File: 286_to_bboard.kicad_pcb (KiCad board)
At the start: 2 copper layers, 33.5 x 78.7 mm, 28 parts, among them J1 Conn_01x30, J2 Conn_01x30, J3 Conn_01x02, U1 74HC244

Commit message: finalize initial design
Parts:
- added C6: C, Capacitor_SMD:C_0805_2012Metric_Pad1.18x1.45mm_HandSolder, F.Cu at (157.7, 70.6)
- C1, C2, C3, C4: footprint Capacitor_SMD:C_0805_2012Metric -> Capacitor_SMD:C_0805_2012Metric_Pad1.18x1.45mm_HandSolder
- C5: footprint Capacitor_SMD:C_0402_1005Metric -> Capacitor_SMD:C_0402_1005Metric_Pad0.74x0.62mm_HandSolder
- J1, J2: footprint Connector_PinSocket_2.54mm:PinSocket_1x30_P2.54mm_Vertical_SMD_Pin1Left -> Connector_PinHeader_2.54mm:PinHeader_1x30_P2.54mm_Vertical_SMD_Pin1Left
- J3: moved to B.Cu
- R9: footprint Resistor_SMD:R_0402_1005Metric -> Resistor_SMD:R_0402_1005Metric_Pad0.72x0.64mm_HandSolder
- moved JP1 1.27 mm to (148.2, 51.1)
- moved C5 0.20 mm to (143.8, 53.6)
- turned J3 to -90 degrees
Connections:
- C1 pad 1: Net-(UA1-CAP) -> VCC
- J1 pad 27: GND -> /CLK
- J1 pad 28: /CLK -> /RESET
- J1 pad 29: VCC -> GND
- J1 pad 30: /RESET -> VCC
- J1 pad 5: /~{S1} -> /M/~{IO}
- J1 pad 6: /~{S0} -> /~{BHE}
- J1 pad 7: /M/~{IO} -> /~{S1}
- J1 pad 8: /~{BHE} -> /~{S0}
- J2 pad 5: GND -> /~{READY}
- J2 pad 6: VCC -> GND
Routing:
- net GND: track 18.0 -> 130.9 mm, vias 0 -> 79
- net /~{BUSY}: track 0.00 -> 54.2 mm, vias 0 -> 1
- net /~{PEACK}: track 0.00 -> 51.0 mm, vias 0 -> 1
- net /~{S1}: track 0.00 -> 49.0 mm, vias 0 -> 3
- net /~{S0}: track 0.00 -> 47.1 mm, vias 0 -> 3
- net /~{ERROR}: track 0.00 -> 45.4 mm, vias 0 -> 1
- net /HLDA: track 0.00 -> 41.9 mm, vias 0 -> 1
- net /~{BHE}: track 0.00 -> 41.1 mm, vias 0 -> 3
- net /A0: track 0.00 -> 38.6 mm, vias 0 -> 1
- net /M/~{IO}: track 0.00 -> 38.0 mm, vias 0 -> 3
- net /COD/~{INTA}: track 0.00 -> 37.9 mm, vias 0 -> 3
- net VCC: track 100.9 -> 136.7 mm, vias 4 -> 5
- net /~{LOCK}: track 0.00 -> 33.0 mm, vias 0 -> 3
- net /A2: track 0.00 -> 32.7 mm, vias 0 -> 1
- net /A1: track 0.00 -> 32.0 mm, vias 0 -> 1
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- added copper zone on B.Cu, net GND
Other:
- board text added: "HOLD"
- board text added: "INTR"
- board text added: "NMI"
- board text added: "PEREQ"
- board text added: "~{READY}"

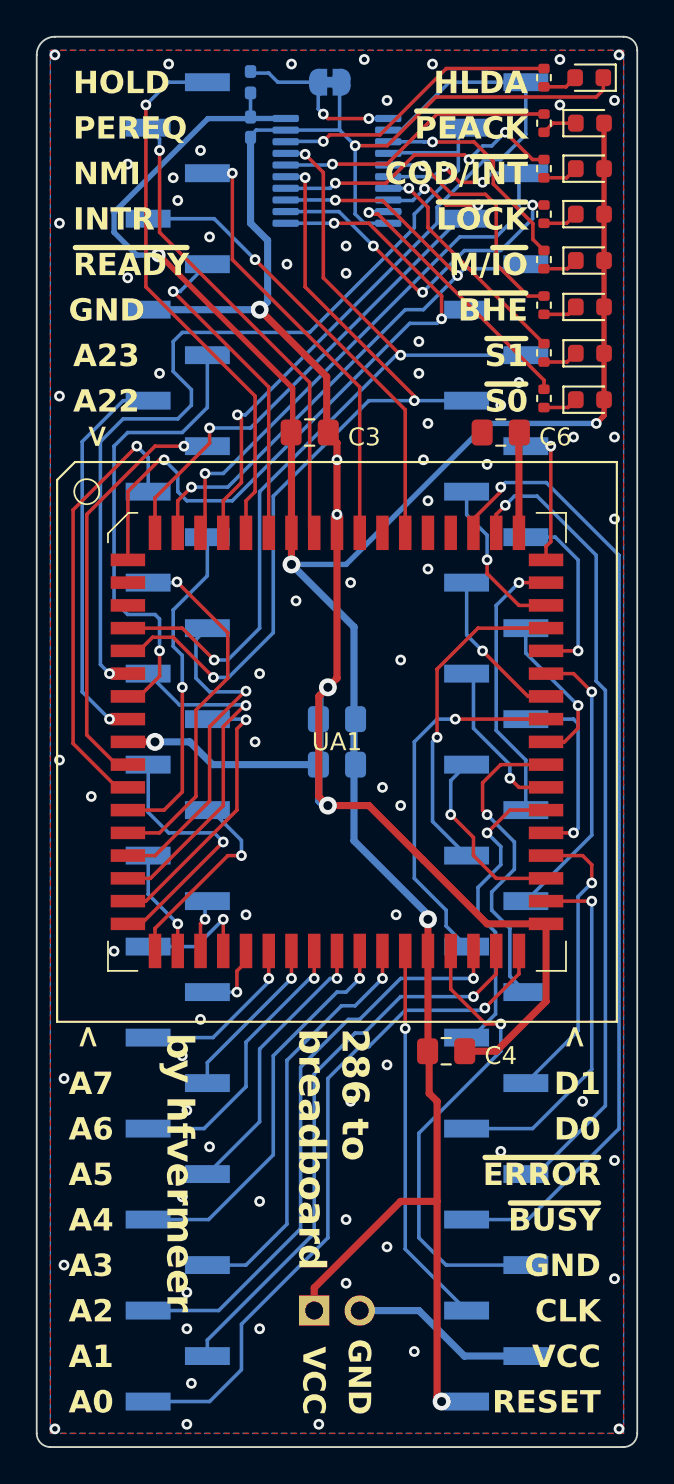
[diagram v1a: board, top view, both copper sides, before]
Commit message: strengthen headers with riveting vias
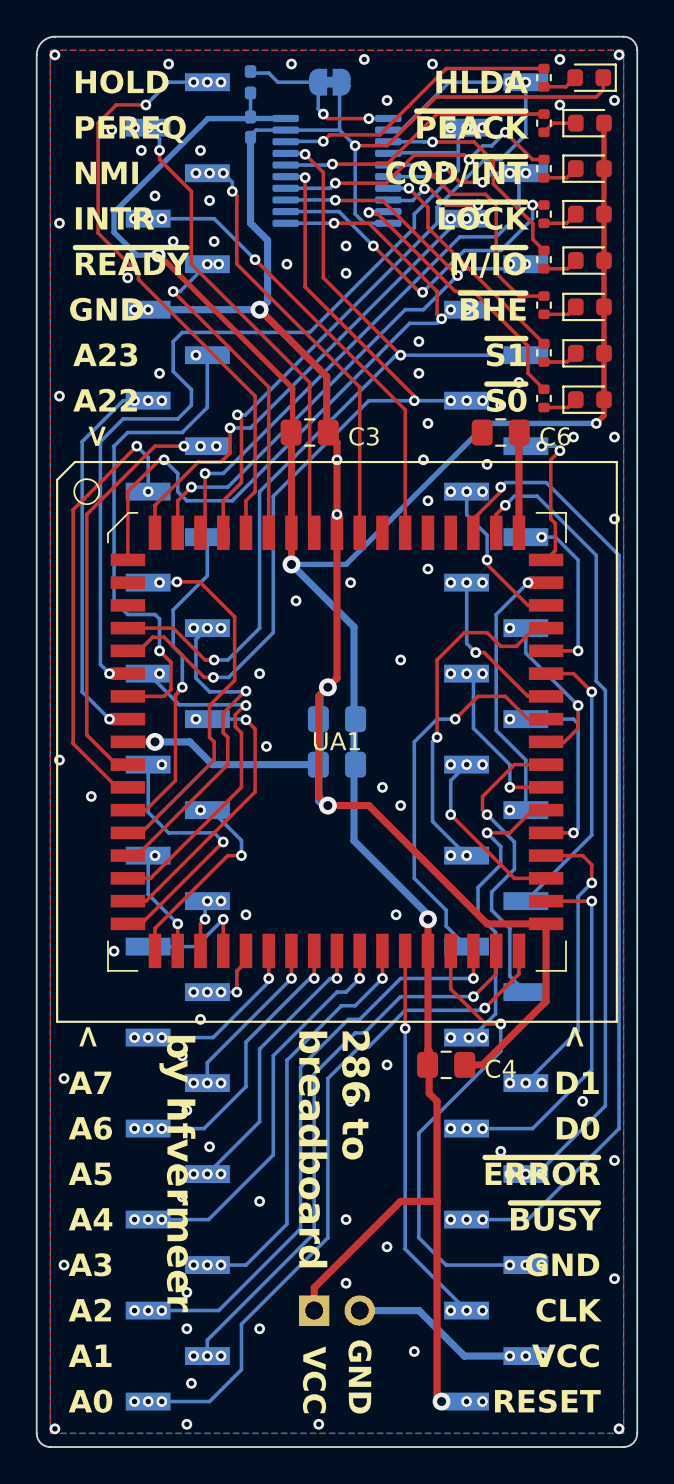
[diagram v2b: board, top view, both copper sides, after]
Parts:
- moved C4 0.76 mm to (154.7, 105.9)
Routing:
- net /HOLD: track 30.6 -> 33.8 mm, vias 1 -> 4
- net /A23: track 26.0 -> 27.4 mm, vias 1 -> 2
- net /D4: track 20.5 -> 21.6 mm
- net /D6: track 18.3 -> 19.3 mm, vias 1 -> 3
- net /D15: track 7.86 -> 8.64 mm, vias 1 -> 2
- net /A18: track 20.2 -> 20.8 mm, vias 1 -> 2
- net Net-(U1-2Y3): track 16.0 -> 16.6 mm
- net /D8: track 10.6 -> 9.96 mm, vias 1 -> 4
- net /A19: track 18.7 -> 18.1 mm
- net /A15: track 15.6 -> 16.0 mm, vias 1 -> 2
- net /A17: track 19.0 -> 18.6 mm, vias 1 -> 4
- net /D7: track 15.4 -> 15.1 mm, vias 1 -> 2
- net /D10: track 9.07 -> 9.37 mm, vias 1 -> 4
- net /D14: track 9.07 -> 8.77 mm, vias 1 -> 4
- net /NMI: track 24.4 -> 24.1 mm, vias 1 -> 4
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
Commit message: add anchor plates
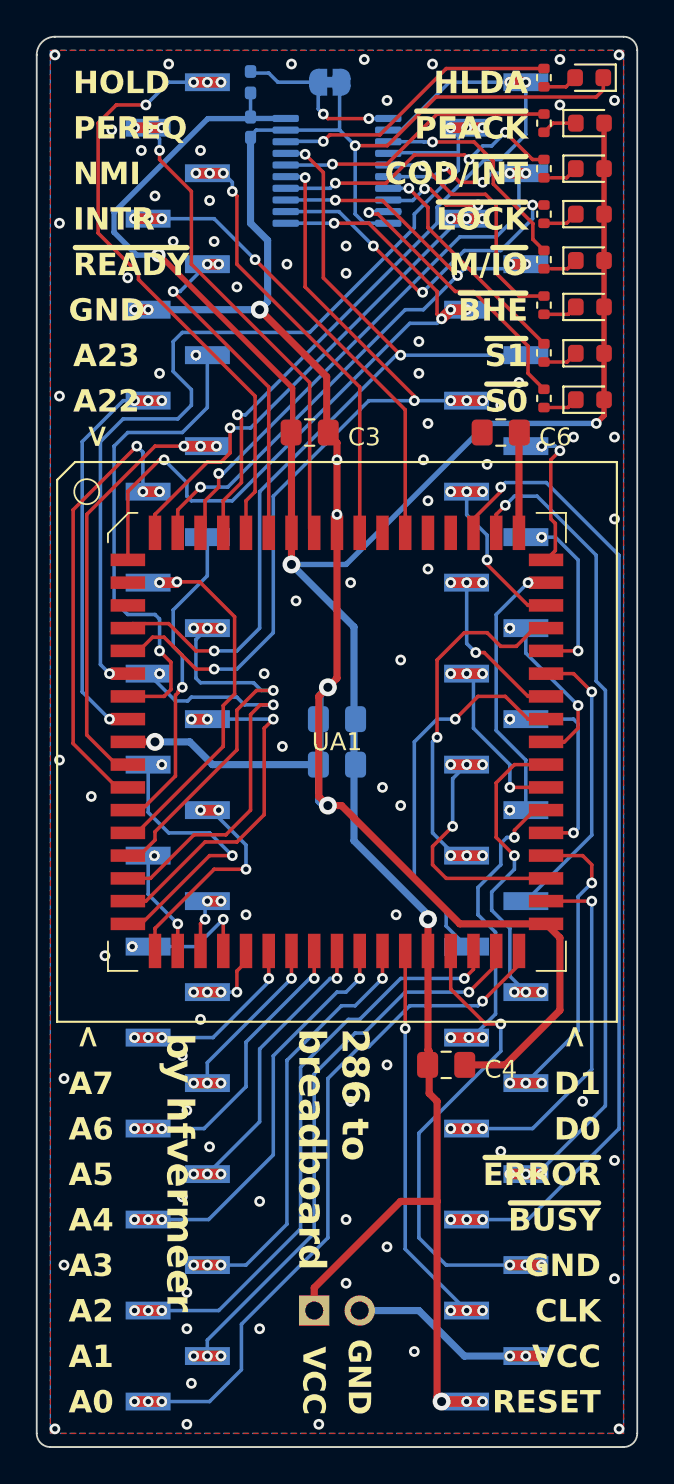
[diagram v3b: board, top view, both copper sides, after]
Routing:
- net /D8: track 9.96 -> 14.8 mm
- net /A17: track 18.6 -> 22.7 mm
- net GND: track 131.1 -> 135.0 mm, vias 86 -> 87
- net /A15: track 16.0 -> 19.7 mm, vias 2 -> 3
- net /A16: track 19.7 -> 23.1 mm
- net /D6: track 19.3 -> 21.4 mm, vias 3 -> 4
- net /A13: track 11.2 -> 13.0 mm, vias 2 -> 3
- net /A21: track 23.6 -> 25.4 mm
- net /~{ERROR}: track 45.4 -> 47.1 mm
- net /D1: track 16.5 -> 18.3 mm
- net /CLK: track 26.2 -> 27.9 mm
- net /~{PEACK}: track 51.0 -> 52.7 mm
- net /~{BUSY}: track 54.2 -> 56.0 mm
- net /RESET: track 21.5 -> 23.3 mm
- net /D14: track 8.77 -> 10.6 mm
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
